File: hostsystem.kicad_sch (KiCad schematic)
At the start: 34 parts, among them J1001 TC2050, J1002 Conn_01x03_Pin, U1001 AM6231ASGGGAALW, U1002 FT24C32A-ELR-T, U1004 SN74LVC2G241DCUR, X1001 32.768kHz, X1002 25MHz

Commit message: Fixed ERC errors and warnings (zero errors and zero warnings)
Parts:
- renumbered C1008 to C1005, C1005 to C1006, C1006 to C1007, R1014 to R1001, R1015 to R1002, R1001 to R1003, R1002 to R1004, R1003 to R1005, R1004 to R1006, R1005 to R1007, R1006 to R1008, R1007 to R1009, R1008 to R1010, R1010 to R1011, R1009 to R1012, R1011 to R1013, R1012 to R1014, R1013 to R1015, U1004 to U1002, U1002 to U1003

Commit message: Labeled all nets and added some footprints
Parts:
- U1001: footprint (none) -> AM6231ASGGGAALW:BGA425C50P25X25_1300X1300X89
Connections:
- net MCU_OSC0_XI: now reaches C1004.1, U1001.B2 (MCU_SPI0_OSC0_XI), X1002.3
- net MCU_OSC0: now reaches R1012.1, U1001.A3 (MCU_SPI0_OSC0_XO)
- net MCU_OSC0_XO: now reaches C1006.1, R1012.2, X1002.1
- net SoC_I2C_SCL: now reaches R1011.1, U1001.B16 (I2C0_SCL)
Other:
- note added: "EEPROM"
- note added: "MCU Domain"
- note added: "OSPI + GPMC (3.3V and 1.8V Banks)"
- note added: "SoC Communication"
- note added: "SoC JTAG"
- note added: "SoC System"
- note added: "SoC UART Header Pins"
- note added: "WKUP Domain"
- note removed: "Maybe place header pins for MCU_UART"
- moved on the sheet: C1001, C1002, C1003, C1004, C1005, C1006, C1007, D1001, D1002, D1003, J1001, J1002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

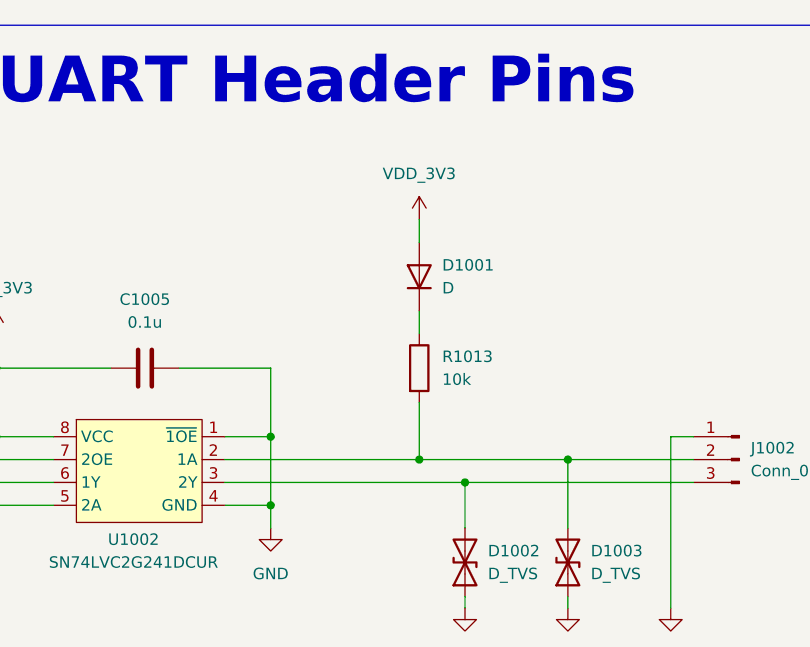
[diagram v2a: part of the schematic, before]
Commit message: Added more IC footprints
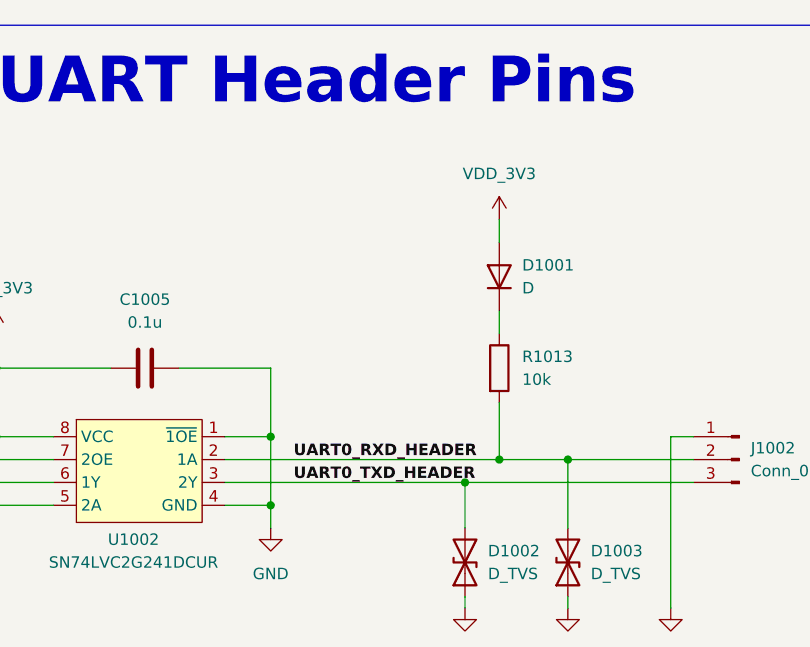
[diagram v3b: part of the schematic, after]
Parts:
- U1002: footprint (none) -> SN74LVC2G241DCUR:SOP50P310X90-8N
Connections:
- net UART0_TXD_HEADER: now reaches D1002.2 (A2), J1002.3 (Pin_3), U1002.3 (2Y)
- net UART0_RXD_HEADER: now reaches D1003.2 (A2), J1002.2 (Pin_2), R1013.2, U1002.2 (1A)
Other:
- moved on the sheet: D1001, R1013
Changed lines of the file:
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@@
 	)
 	(junction
-		(at 450.85 407.67)
-		(diameter 0)
-		(color 0 0 0 0)
-	)
-	(junction
 		(at 190.5 313.69)
 		(diameter 0)
@@
 		(color 0 0 0 0)
 	)
+	(junction
+		(at 459.74 407.67)
+		(diameter 0)
+		(color 0 0 0 0)
+	)
 	(no_connect
 		(at 544.83 294.64)
@@
 	(wire
 		(pts
-			(xy 450.85 401.32) (xy 450.85 407.67)
+			(xy 459.74 401.32) (xy 459.74 407.67)
 		)
 		(stroke
@@
 	(wire
 		(pts
-			(xy 450.85 381) (xy 450.85 383.54)
+			(xy 459.74 381) (xy 459.74 383.54)
 		)
 		(stroke
@@
 	(wire
 		(pts
-			(xy 450.85 407.67) (xy 429.26 407.67)
+			(xy 429.26 407.67) (xy 459.74 407.67)
 		)
 		(stroke
@@
 	(wire
 		(pts
+			(xy 459.74 407.67) (xy 467.36 407.67)
+		)
+		(stroke
+			(width 0)
+			(type default)
+		)
+	)
+	(wire
+		(pts
 			(xy 455.93 410.21) (xy 481.33 410.21)
 		)
@@
 	(wire
 		(pts
-			(xy 450.85 407.67) (xy 467.36 407.67)
-		)
-		(stroke
-			(width 0)
-			(type default)
-		)
-	)
-	(wire
-		(pts
 			(xy 270.51 196.85) (xy 290.83 196.85)
 		)
@@
 	(wire
 		(pts
-			(xy 450.85 391.16) (xy 450.85 393.7)
+			(xy 459.74 391.16) (xy 459.74 393.7)
 		)
 		(stroke
@@
 		)
 	)
+	(label "UART0_TXD_HEADER"
+		(at 436.88 410.21 0)
+		(effects
+			(font
+				(size 1.27 1.27)
+				(thickness 0.254)
+				(bold yes)
+			)
+			(justify left bottom)
+		)
+	)
 	(label "SOC_TDO"
 		(at 115.57 406.4 180)
@@
 		)
 	)
+	(label "UART0_RXD_HEADER"
+		(at 436.88 407.67 0)
+		(effects
+			(font
+				(size 1.27 1.27)
+				(thickness 0.254)
+				(bold yes)
+			)
+			(justify left bottom)
+		)
+	)
 	(label "EEP_WP"
 		(at 351.79 414.02 180)
@@
 	(symbol
 		(lib_id "power:VDD")
-		(at 450.85 381 0)
+		(at 459.74 381 0)
 		(unit 1)
 		(exclude_from_sim no)
@@
 		(fields_autoplaced yes)
 		(property "Reference" "#PWR01012"
-			(at 450.85 384.81 0)
+			(at 459.74 384.81 0)
 			(effects
 				(font
@@
 		)
 		(property "Value" "VDD_3V3"
-			(at 450.85 375.92 0)
+			(at 459.74 375.92 0)
 			(effects
 				(font
@@
 		)
 		(property "Footprint" ""
-			(at 450.85 381 0)
+			(at 459.74 381 0)
 			(effects
 				(font
@@
 		)
 		(property "Datasheet" ""
-			(at 450.85 381 0)
+			(at 459.74 381 0)
 			(effects
 				(font
@@
 		)
 		(property "Description" "Power symbol creates a global label with name \"VDD\""
-			(at 450.85 381 0)
+			(at 459.74 381 0)
 			(effects
 				(font
@@
 	(symbol
 		(lib_id "Device:R")
-		(at 450.85 397.51 0)
+		(at 459.74 397.51 0)
 		(unit 1)
 		(exclude_from_sim no)
@@
 		(fields_autoplaced yes)
 		(property "Reference" "R1013"
-			(at 453.39 396.2399 0)
+			(at 462.28 396.2399 0)
 			(effects
 				(font
@@
 		)
 		(property "Value" "10k"
-			(at 453.39 398.7799 0)
+			(at 462.28 398.7799 0)
 			(effects
 				(font
@@
 		)
 		(property "Footprint" ""
-			(at 449.072 397.51 90)
+			(at 457.962 397.51 90)
 			(effects
 				(font
@@
 		)
 		(property "Datasheet" "~"
-			(at 450.85 397.51 0)
+			(at 459.74 397.51 0)
 			(effects
 				(font
@@
 		)
 		(property "Description" "Resistor"
-			(at 450.85 397.51 0)
+			(at 459.74 397.51 0)
 			(effects
 				(font
@@
 	(symbol
 		(lib_id "Device:D")
-		(at 450.85 387.35 90)
+		(at 459.74 387.35 90)
 		(unit 1)
 		(exclude_from_sim no)
@@
 		(fields_autoplaced yes)
 		(property "Reference" "D1001"
-			(at 453.39 386.0799 90)
+			(at 462.28 386.0799 90)
 			(effects
 				(font
@@
 		)
 		(property "Value" "D"
-			(at 453.39 388.6199 90)
+			(at 462.28 388.6199 90)
 			(effects
 				(font
@@
 		)
 		(property "Footprint" ""
-			(at 450.85 387.35 0)
+			(at 459.74 387.35 0)
 			(effects
 				(font
@@
 		)
 		(property "Datasheet" "~"
-			(at 450.85 387.35 0)
+			(at 459.74 387.35 0)
 			(effects
 				(font
@@
 		)
 		(property "Description" "Diode"
-			(at 450.85 387.35 0)
+			(at 459.74 387.35 0)
 			(effects
 				(font
@@
 		)
 		(property "Sim.Device" "D"
-			(at 450.85 387.35 0)
+			(at 459.74 387.35 0)
 			(effects
 				(font
@@
 		)
 		(property "Sim.Pins" "1=K 2=A"
-			(at 450.85 387.35 0)
+			(at 459.74 387.35 0)
 			(effects
 				(font
@@
 			)
 		)
-		(property "Footprint" ""
+		(property "Footprint" "SN74LVC2G241DCUR:SOP50P310X90-8N"
 			(at 419.1 408.94 0)
 			(effects

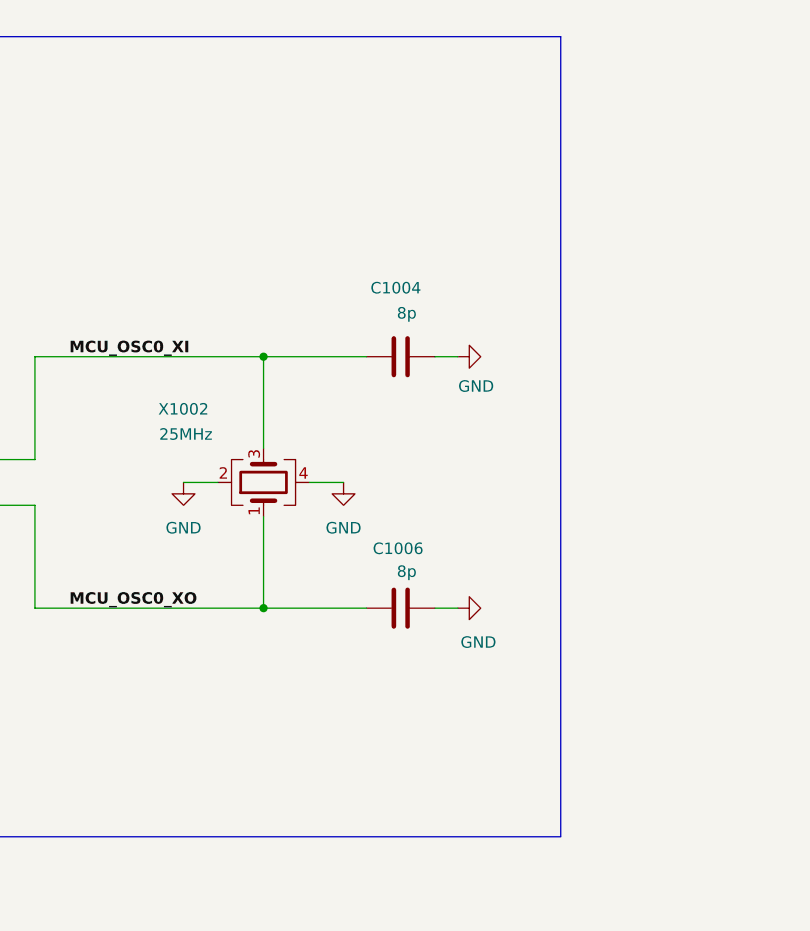
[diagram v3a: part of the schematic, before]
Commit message: Added many more footprints
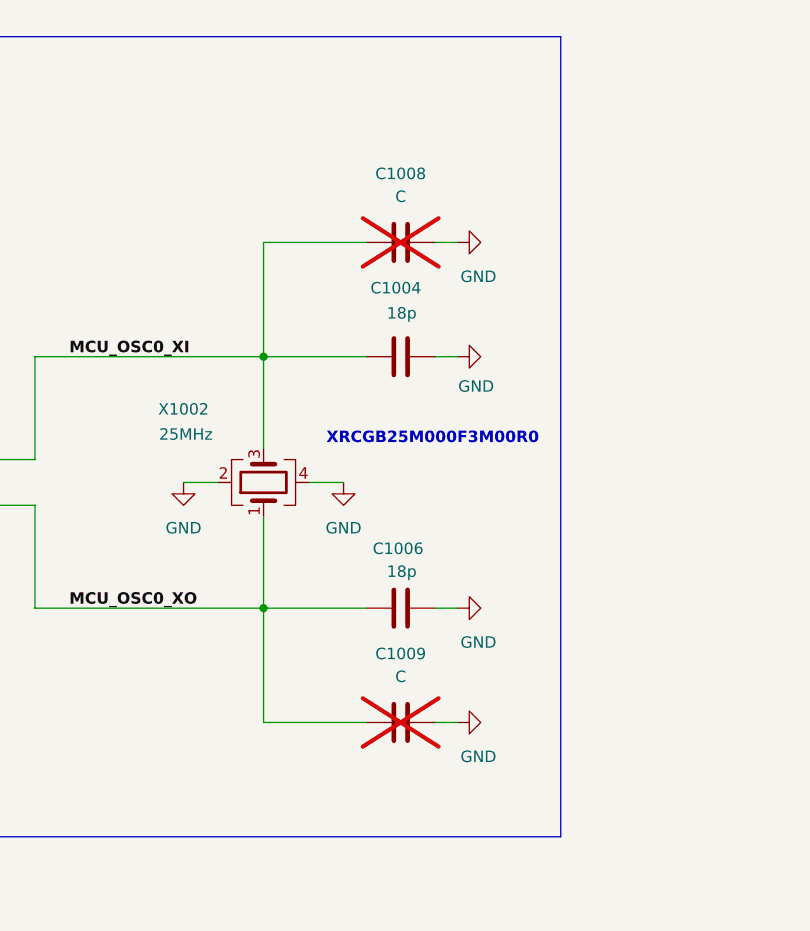
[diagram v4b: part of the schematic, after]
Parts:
- added C1008, C1009: C, symbol Device:C
- C1004, C1006: value 8p -> 18p
- X1001: footprint (none) -> SoftServicesFootprintLibrary:FC-135R 32.7680KA-A3
- X1002: footprint (none) -> Crystal:Crystal_SMD_2016-4Pin_2.0x1.6mm
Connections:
- net GND: now also C1008.2, C1009.2
- net MCU_OSC0_XI: now also C1008.1
- net MCU_OSC0_XO: now also C1009.1
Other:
- note added: "XRCGB25M000F3M00R0"

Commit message: More footprints
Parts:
- removed U1003: FT24C32A-ELR-T, symbol SoftServicesSymbolLibrary:FT24C32A-ELR-T
- added U1003: AT24C32D-STUM-T, Package_TO_SOT_SMD:SOT-23-5, symbol SoftServicesSymbolLibrary:AT24C32D-STUM-T
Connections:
- net EEP_WP: now also U1003.5 (WP)
- net GND: now also U1003.2 (VSS)
- net I2C0_SCL: now also U1003.1 (SCL)
- net I2C0_SDA: now also U1003.3 (SDA)
- net VDD_3V3: now also U1003.4 (VCC)
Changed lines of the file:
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@@
 	)
 	(symbol
+		(lib_id "SoftServicesSymbolLibrary:AT24C32D-STUM-T")
+		(at 309.88 411.48 0)
+		(unit 1)
+		(exclude_from_sim no)
+		(in_bom yes)
+		(on_board yes)
+		(dnp no)
+		(fields_autoplaced yes)
+		(property "Reference" "U1003"
+			(at 311.785 397.51 0)
+			(effects
+				(font
+					(size 1.27 1.27)
+				)
+			)
+		)
+		(property "Value" "AT24C32D-STUM-T"
+			(at 311.785 400.05 0)
+			(effects
+				(font
+					(size 1.27 1.27)
+				)
+			)
+		)
+		(property "Footprint" "Package_TO_SOT_SMD:SOT-23-5"
+			(at 309.88 411.48 0)
+			(effects
+				(font
+					(size 1.27 1.27)
+				)
+				(hide yes)
+			)
+		)
+		(property "Datasheet" ""
+			(at 309.88 411.48 0)
+			(effects
+				(font
+					(size 1.27 1.27)
+				)
+				(hide yes)
+			)
+		)
+		(property "Description" ""
+			(at 309.88 411.48 0)
+			(effects
+				(font
+					(size 1.27 1.27)
+				)
+				(hide yes)
+			)
+		)
+		(pin "5"
+		)
+		(pin "3"
+		)
+		(pin "2"
+		)
+		(pin "1"
+		)
+		(pin "4"
+		)
+		(instances
+			(project ""
+				(path "/b43b7bca-e50d-42ec-8ff0-e0016dfefe0a/5bbf73b3-d883-47e7-ac01-c5b0358ac807"
+					(reference "U1003")
+					(unit 1)
+				)
+			)
+		)
+	)
+	(symbol
 		(lib_id "Device:R")
 		(at 227.33 388.62 0)
@@
 					(unit 1)
 				)
-			)
-		)
-	)
-	(symbol
-		(lib_id "SoftServicesSymbolLibrary:FT24C32A-ELR-T")
-		(at 309.88 411.48 0)
-		(unit 1)
-		(exclude_from_sim no)
-		(in_bom yes)
-		(on_board yes)
-		(dnp no)
-		(fields_autoplaced yes)
-		(property "Reference" "U1003"
-			(at 311.785 397.51 0)
-			(effects
-				(font
-					(size 1.27 1.27)
-				)
-			)
-		)
-		(property "Value" "FT24C32A-ELR-T"
-			(at 311.785 400.05 0)
-			(effects
-				(font
-					(size 1.27 1.27)
-				)
-			)
-		)
-		(property "Footprint" ""
-			(at 309.88 411.48 0)
-			(effects
-				(font
-					(size 1.27 1.27)
-				)
-				(hide yes)
-			)
-		)
-		(property "Datasheet" ""
-			(at 309.88 411.48 0)
-			(effects
-				(font
-					(size 1.27 1.27)
-				)
-				(hide yes)
-			)
-		)
-		(property "Description" ""
-			(at 309.88 411.48 0)
-			(effects
-				(font
-					(size 1.27 1.27)
-				)
-				(hide yes)
-			)
-		)
-		(pin "1"
-		)
-		(pin "3"
-		)
-		(pin "4"
-		)
-		(pin "2"
-		)
-		(pin "5"
-		)
-		(instances
-			(project ""
-				(path "/b43b7bca-e50d-42ec-8ff0-e0016dfefe0a/5bbf73b3-d883-47e7-ac01-c5b0358ac807"
-					(reference "U1003")
-					(unit 1)
-				)

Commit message: Finished IC and crystal footprints
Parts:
- J1002: footprint (none) -> Connector_PinHeader_2.54mm:PinHeader_1x03_P2.54mm_Vertical
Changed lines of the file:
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@@
 			)
 		)
-		(property "Footprint" ""
+		(property "Footprint" "Connector_PinHeader_2.54mm:PinHeader_1x03_P2.54mm_Vertical"
 			(at 486.41 407.67 0)
 			(effects
